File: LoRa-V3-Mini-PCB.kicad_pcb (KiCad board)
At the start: 2 copper layers, 52 x 18 mm, 24 parts, among them Q1 NA, SW1 Application Button, SW2 MCU Reset, U1 Lora-E5, U2 BR24G1MFVT, U3 SHT40, U4 TSL25911

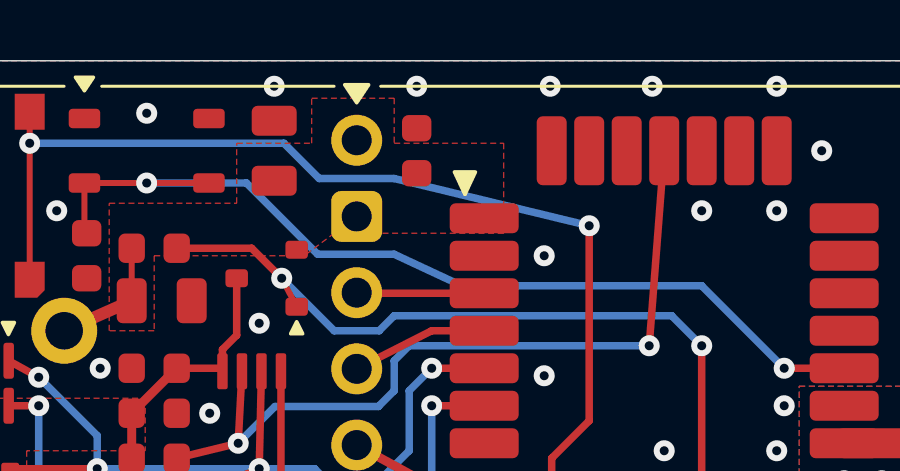
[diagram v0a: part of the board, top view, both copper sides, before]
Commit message: move decouple cap closer to MCU
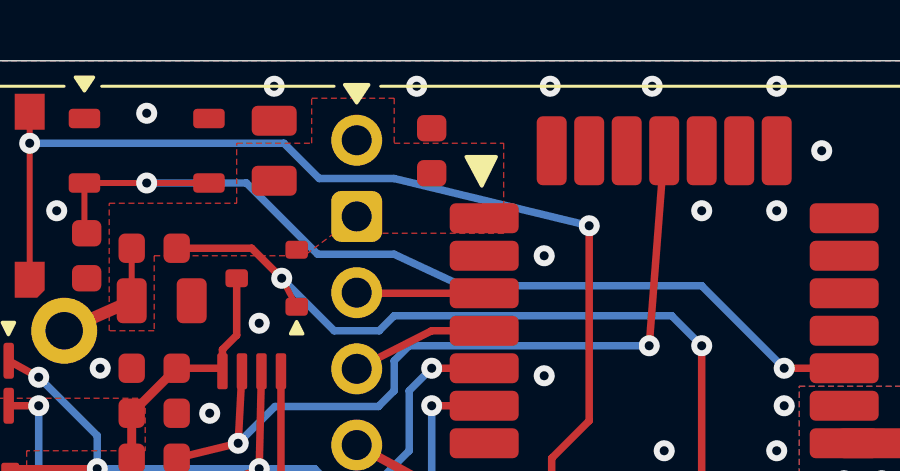
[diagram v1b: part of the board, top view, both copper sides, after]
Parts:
- moved C3 0.50 mm to (145.2, 97.5)
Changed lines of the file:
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@@
 		)
 	)
+	(property "majorVersion" "0")
+	(property "minorVersion" "4")
+	(property "releaseDate" "Mon Feb 24 16:18:53 2025")
+	(property "releaseDateShort" "2025-02-24")
 	(net 0 "")
 	(net 1 "GND")
@@
 		(sheetname "Root")
 		(sheetfile "LoRa-V3-Mini-PCB.kicad_sch")
-		(attr through_hole)
+		(attr through_hole exclude_from_bom)
 		(fp_poly
 			(pts
@@
 	(footprint "1projectLibrary:C_0603_nominal"
 		(layer "F.Cu")
-		(at 144.66 97.5 90)
+		(at 145.16 97.5 90)
 		(descr "Capacitor SMD 0603 (1608 Metric), square (rectangular) end terminal, IPC_7351 nominal, (Body size source: IPC-SM-782 page 76, https://www.pcb-3d.com/wordpress/wp-content/uploads/ipc-sm-782a_amendment_1_and_2.pdf), generated with kicad-footprint-generator")
 		(tags "capacitor")
@@
 		(fp_poly
 			(pts
-				(xy -6.992335 -5.293248) (xy -6.292153 -5.293248) (xy -6.642153 -4.543248)
+				(xy -6.6 -5.8) (xy -5.6 -5.8) (xy -6.080373 -4.827772)
 			)
 			(stroke
@@
 			(layer "F.SilkS")
 		)
-		(fp_rect
-			(start -7.5 -7.5)
-			(end 7.5 7.5)
+		(fp_poly
+			(pts
+				(xy -4.5 -7.5) (xy 4.5 -7.5) (xy 4.5 -4.5) (xy 7.5 -4.5) (xy 7.5 4.5) (xy 4.5 4.5) (xy 4.5 7.5)
+				(xy -4.5 7.5) (xy -4.5 4.5) (xy -7.5 4.5) (xy -7.5 -4.5) (xy -4.5 -4.5)
+			)
 			(stroke
 				(width 0.05)
-				(type default)
+				(type solid)
 			)
 			(fill none)
@@
 		(fp_poly
 			(pts
-				(xy -6.992335 -5.3) (xy -6.292153 -5.3) (xy -6.642153 -4.543248)
+				(xy -6.383534 -5.520395) (xy -5.683352 -5.520395) (xy -6.033352 -4.763643)
 			)
 			(stroke
@@
 			(layer "User.1")
 		)
+		(fp_rect
+			(start -7.5 -7.5)
+			(end 7.5 7.5)
+			(stroke
+				(width 0.05)
+				(type default)
+			)
+			(fill none)
+			(layer "User.8")
+		)
 		(pad "1" smd roundrect
 			(at -6 -3.75 90)
@@
 			)
 			(height 4.572)
-			(gr_text "7.0866 mm"
+			(gr_text "7,0866 mm"
 				(at 127.188 107.0433 90)
 				(layer "User.2")
@@
 			)
 			(height 4.572)
-			(gr_text "34.5440 mm"
+			(gr_text "34,5440 mm"
 				(at 147.642 89.65 0)
 				(layer "User.2")
@@
 			)
 			(height 4.318)
-			(gr_text "16.2560 mm"
+			(gr_text "16,2560 mm"
 				(at 168.082 103.5 90)
 				(layer "User.2")
@@
 			)
 			(height -5.08)
-			(gr_text "29.4640 mm"
+			(gr_text "29,4640 mm"
 				(at 147.642 97.27 0)
 				(layer "User.2")
@@
 		)
 		(height 3.05)
-		(gr_text "18.0000 mm"
+		(gr_text "18,0000 mm"
 			(at 182.81 103.5 90)
 			(layer "User.2")
@@
 		)
 		(height -3.6)
-		(gr_text "52.0000 mm"
+		(gr_text "52,0000 mm"
 			(at 154.91 89.75 0)
 			(layer "User.2")

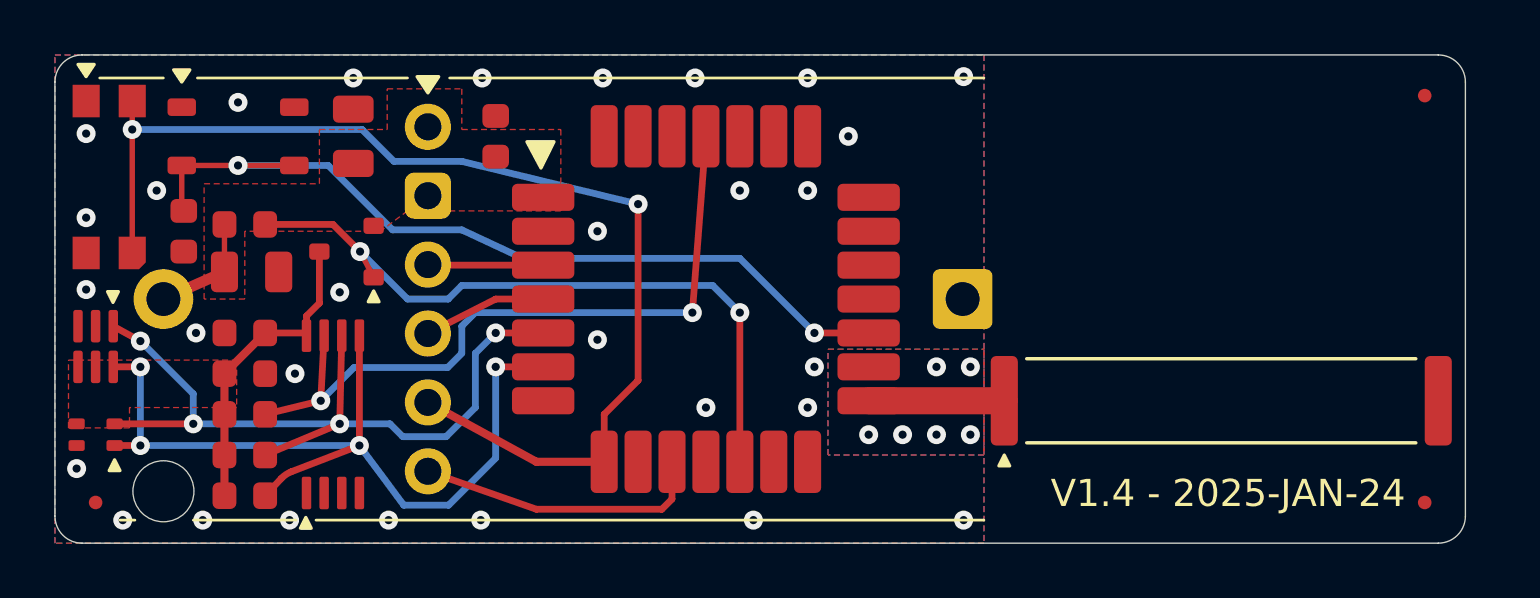
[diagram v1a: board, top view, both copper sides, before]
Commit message: Add Pads for CLI connector
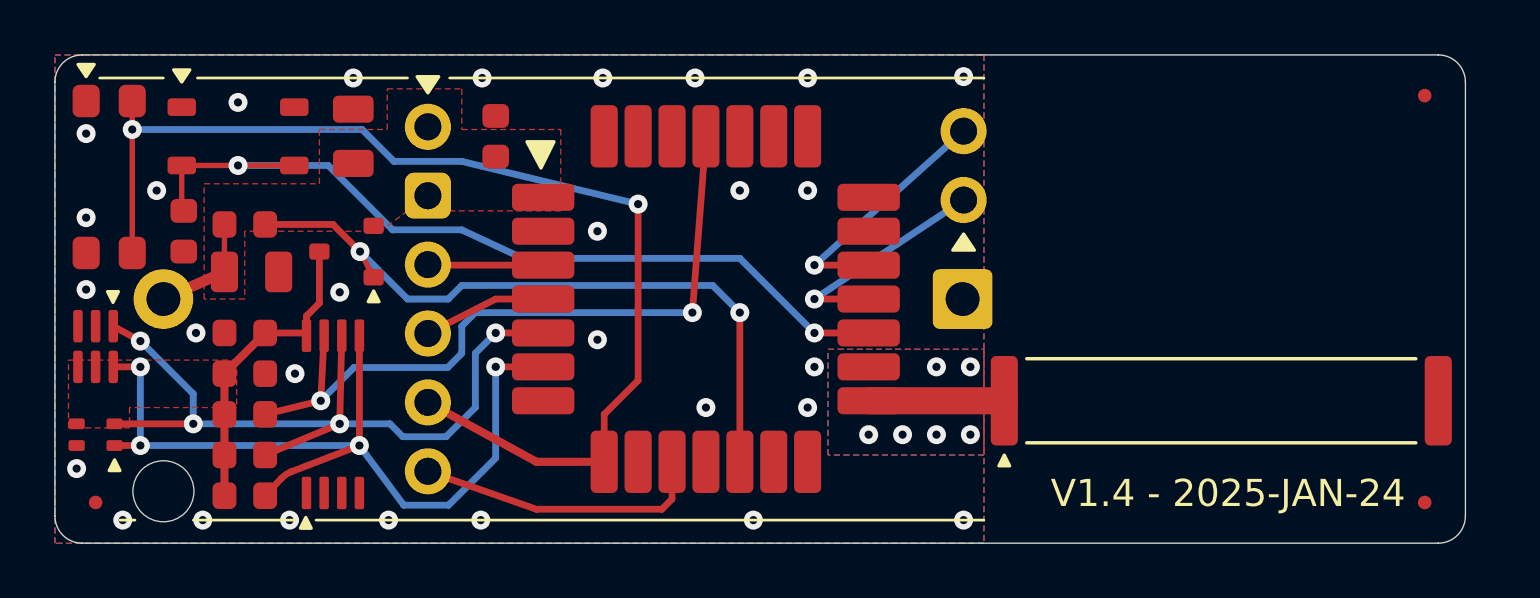
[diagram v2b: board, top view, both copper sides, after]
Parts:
- added CONN2: UART2 - CLI, 1projectLibrary:CliConnector_2p, F.Cu at (162.4, 98.5)
- renumbered CONN5 to CONN1
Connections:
- U1 pad 18: unconnected-(U1-PA3-Pad18) -> UART2-RX
- U1 pad 19: unconnected-(U1-PA2-Pad19) -> UART2-TX
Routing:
- net UART2-TX: track 0.00 -> 9.39 mm, vias 0 -> 1
- net UART2-RX: track 0.00 -> 8.60 mm, vias 0 -> 1
- net GND: vias 36 -> 35
